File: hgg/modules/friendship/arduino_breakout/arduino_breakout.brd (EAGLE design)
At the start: 105.6 x 67.3 mm, 23 parts, among them IC1 MAX481CSA, IC2 MAX481CSA, IC3 74AC165D, IC4 4517, IC5 74AC165D, IC6 74AC165D, IC7 74AC393D, IC8 74AC393D, IC9 74AC393D

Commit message: small routing improvements
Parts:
- moved U$1 0.50 mm to (-0.90, 17.1)
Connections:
- removed net PH6: JP6.9
- new net PH5: JP6.10
- net SLOWTIMESER: now also JP6.9; no longer JP6.10
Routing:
- net GND: track 342.2 -> 346.2 mm
- net PRESENT: track 55.4 -> 56.4 mm
- net N$1: track 10.2 -> 11.2 mm
- net SLOWCLKMOSI: track 59.0 -> 59.5 mm
- net SLOWCLKCLK: track 103.1 -> 103.6 mm
- net PRSNTDATAIN: track 97.5 -> 98.0 mm
- net PPS: track 176.3 -> 176.8 mm
- net N$6: track 51.7 -> 52.2 mm
- net N$5: track 50.8 -> 51.3 mm
- net N$3: track 49.7 -> 50.2 mm
- net N$2: track 49.5 -> 50.0 mm
- net IRQDATAIN: track 100.8 -> 101.3 mm
- net IRQ: track 96.2 -> 96.7 mm
- net INTACKSER: track 87.5 -> 88.0 mm
- net INTACKSCK: track 92.8 -> 93.3 mm
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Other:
- board size 105.6 x 67.3 mm -> 105.6 x 67.9 mm

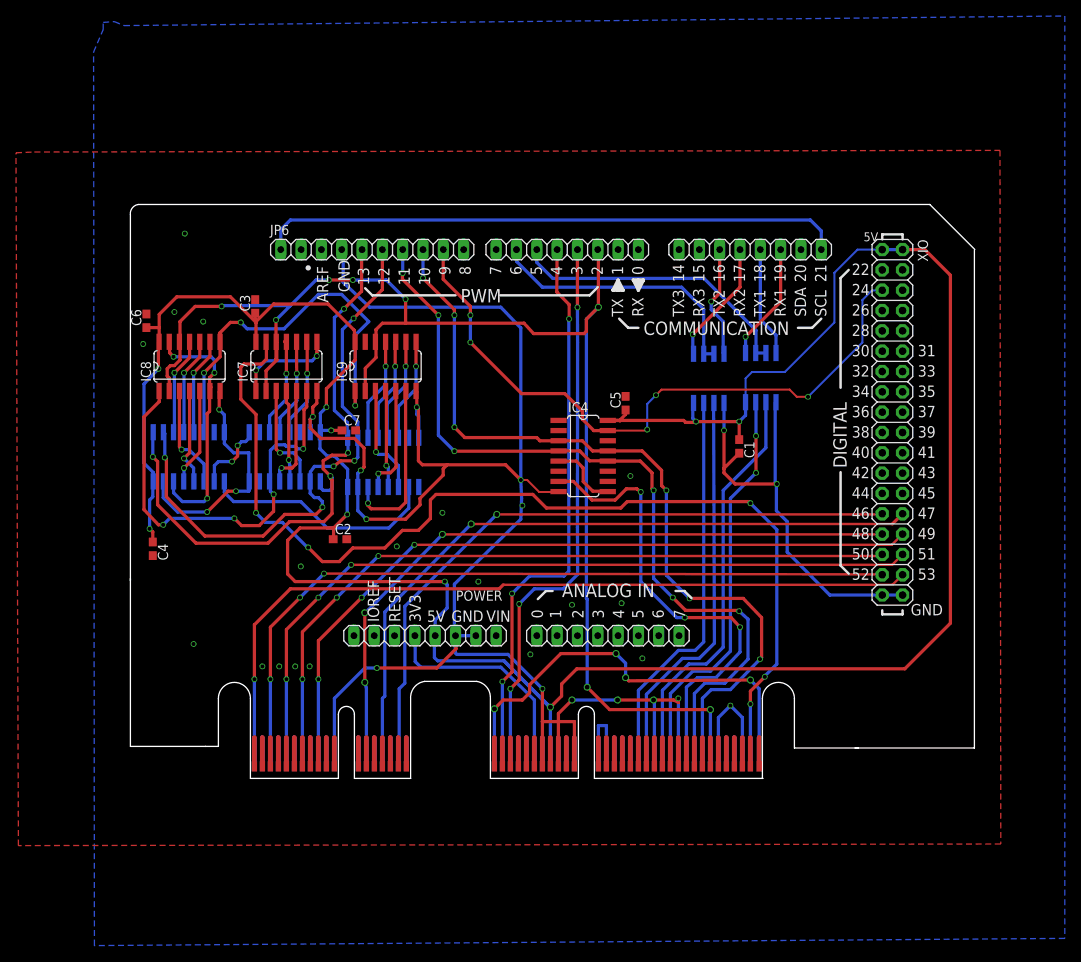
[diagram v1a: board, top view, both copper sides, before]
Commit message: ran DRC, not all passing (PCIe conn), fixed wire width issues, some routing improvements
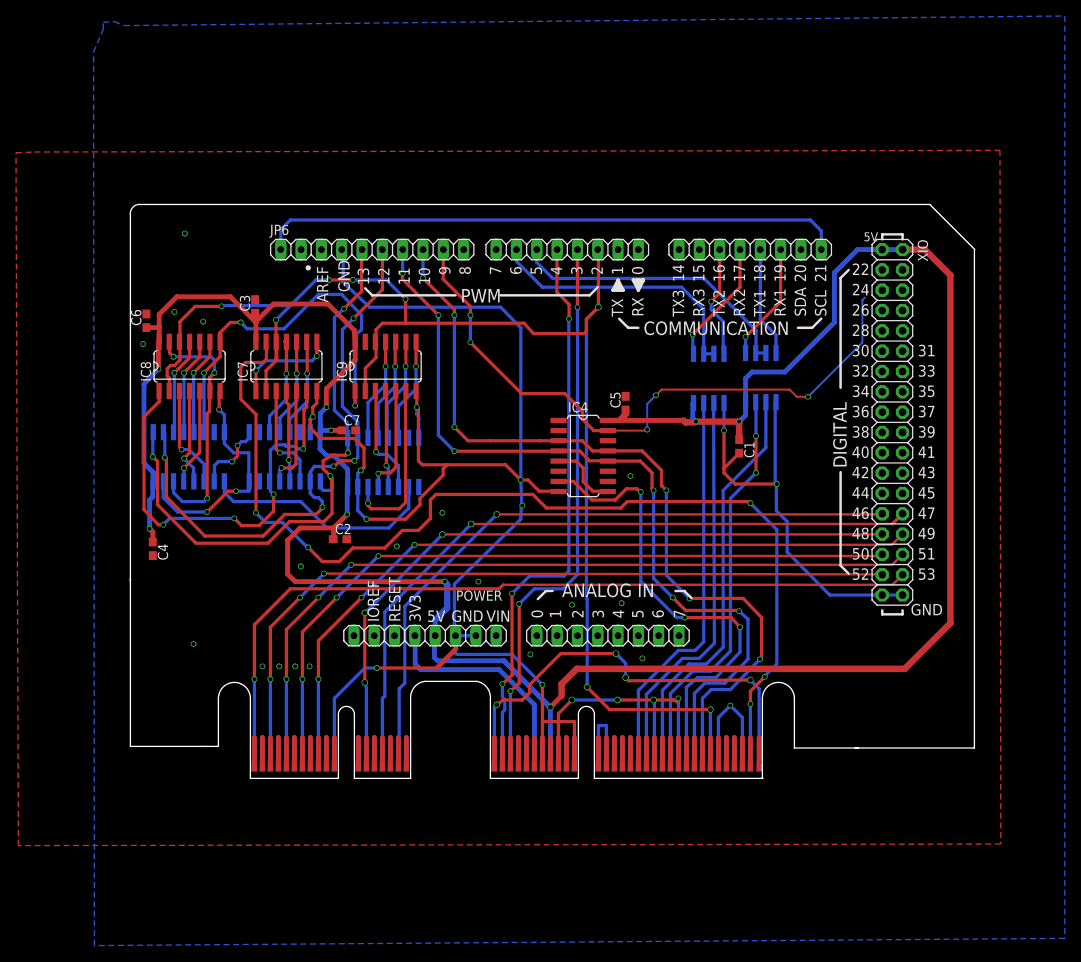
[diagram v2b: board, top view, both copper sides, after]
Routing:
- net SLOWTIMESER: track 82.7 -> 80.1 mm
- net N$27: track 49.3 -> 48.6 mm
